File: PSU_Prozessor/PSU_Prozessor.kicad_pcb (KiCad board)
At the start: 2 copper layers, 192.4 x 77 mm, 85 parts, among them IC1 6N138S, J1 ACJS-MHOP, J2 Conn_01x06, J3 FC68148S, J4 USB2066-05-RBHM-15-STB-00-01-A, J7 USB2066-05-RBHM-15-STB-00-01-A, Q1 BC847, Q2 2N7002, Q3 BC847, Q4 2N7002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

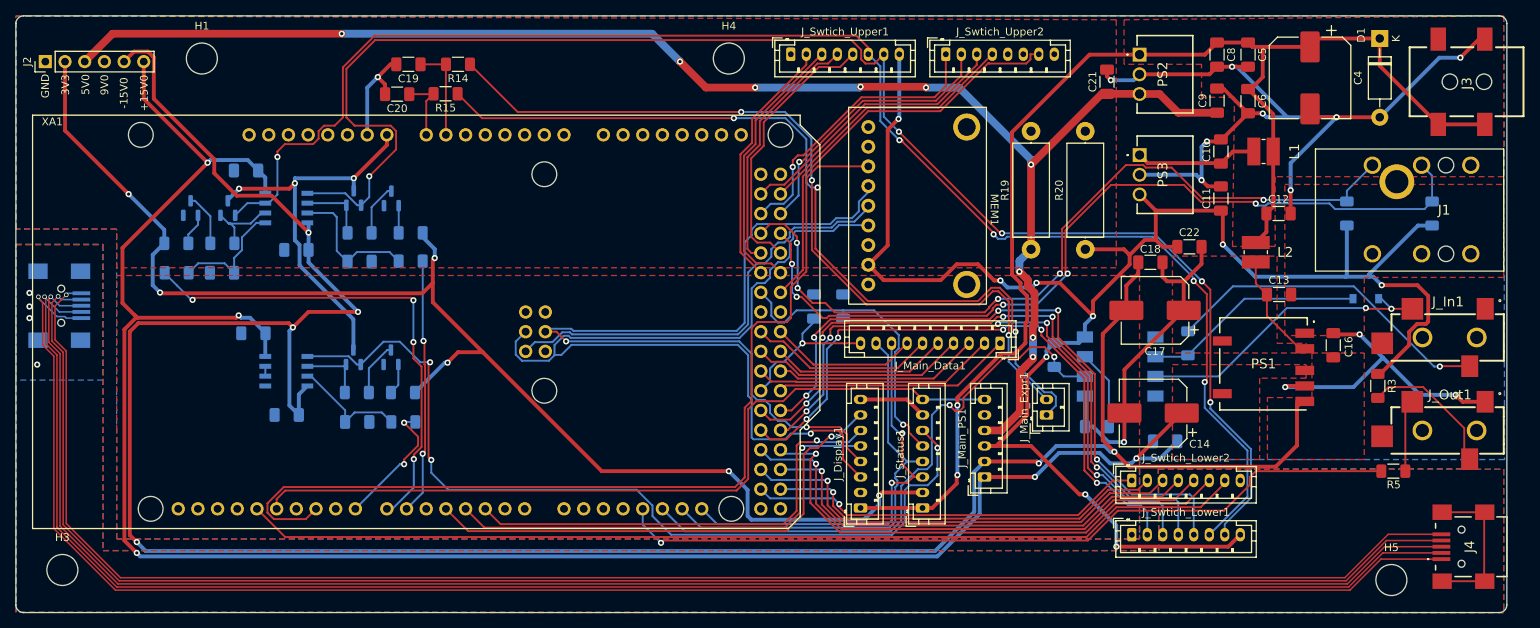
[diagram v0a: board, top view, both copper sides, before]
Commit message: Added 9V supply on PSU for LEDs on switch. Changed FRAM supply
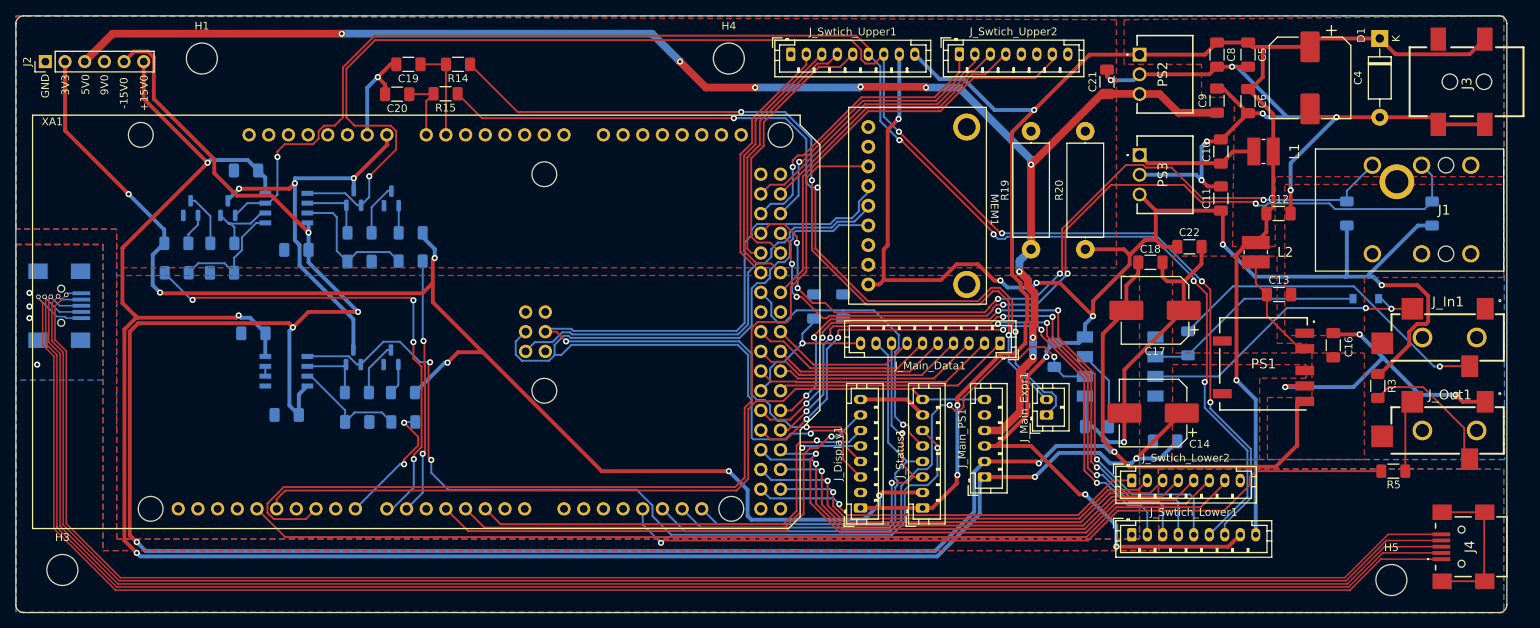
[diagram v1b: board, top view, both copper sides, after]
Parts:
- J_Swtich_Lower1, J_Swtich_Upper1: value Conn_01x08 -> Conn_01x09; footprint Connector_JST:JST_PH_B8B-PH-K_1x08_P2.00mm_Vertical -> Connector_JST:JST_PH_B9B-PH-K_1x09_P2.00mm_Vertical
- moved J_Swtich_Upper2 1.75 mm to (167.8, 67.4)
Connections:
- J3 pad 1: /VDD9V0 -> GND
- J3 pad 2: /VDD9V0 -> GND
- J3 pad 4: GND -> /VDD9V0
- MEM1 pad 8: /VDD3V3 -> unconnected-(MEM1-Pad8)
- MEM1 pad 9: unconnected-(MEM1-Pad9) -> /VDD3V3
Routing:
- net /VDD9V0: track 217.4 -> 271.1 mm, vias 5 -> 7
- net GND: track 217.1 -> 214.1 mm, vias 13 -> 12
- net /OE_Upper: track 53.6 -> 55.4 mm
- net /SW10: track 34.8 -> 36.5 mm
- net /SW9: track 36.1 -> 37.1 mm
- net /SW7: track 37.4 -> 38.1 mm
- net /SW8: track 35.9 -> 36.7 mm
- net /VDD3V3: track 402.3 -> 402.9 mm

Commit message: Changed FRAM pinout, 9V center negative
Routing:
- net /CS_Fram: track 124.1 -> 137.4 mm
- net /VDD3V3: track 402.9 -> 393.1 mm
- net /MOSI: track 109.2 -> 118.7 mm
- net /SCK: track 118.4 -> 124.1 mm

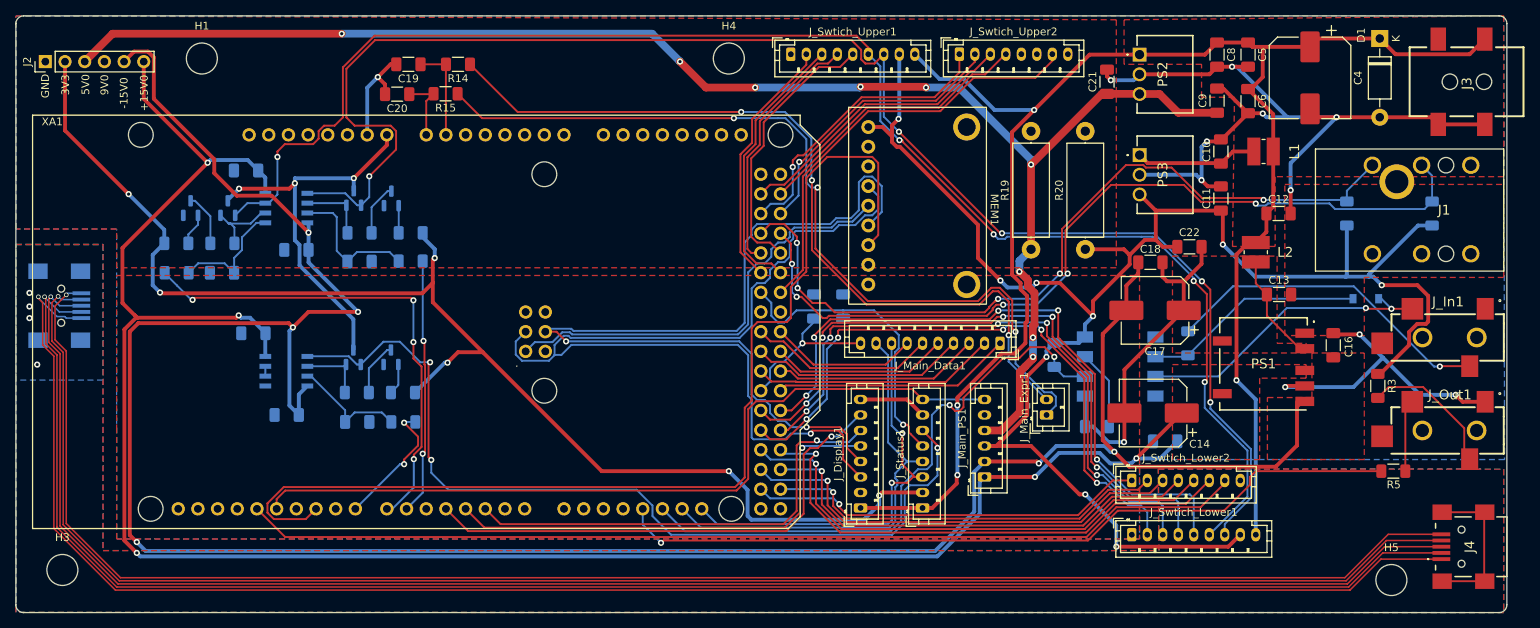
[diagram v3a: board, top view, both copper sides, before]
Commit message: Changed PSU_Processor PCB to adapt changes on Main PCB
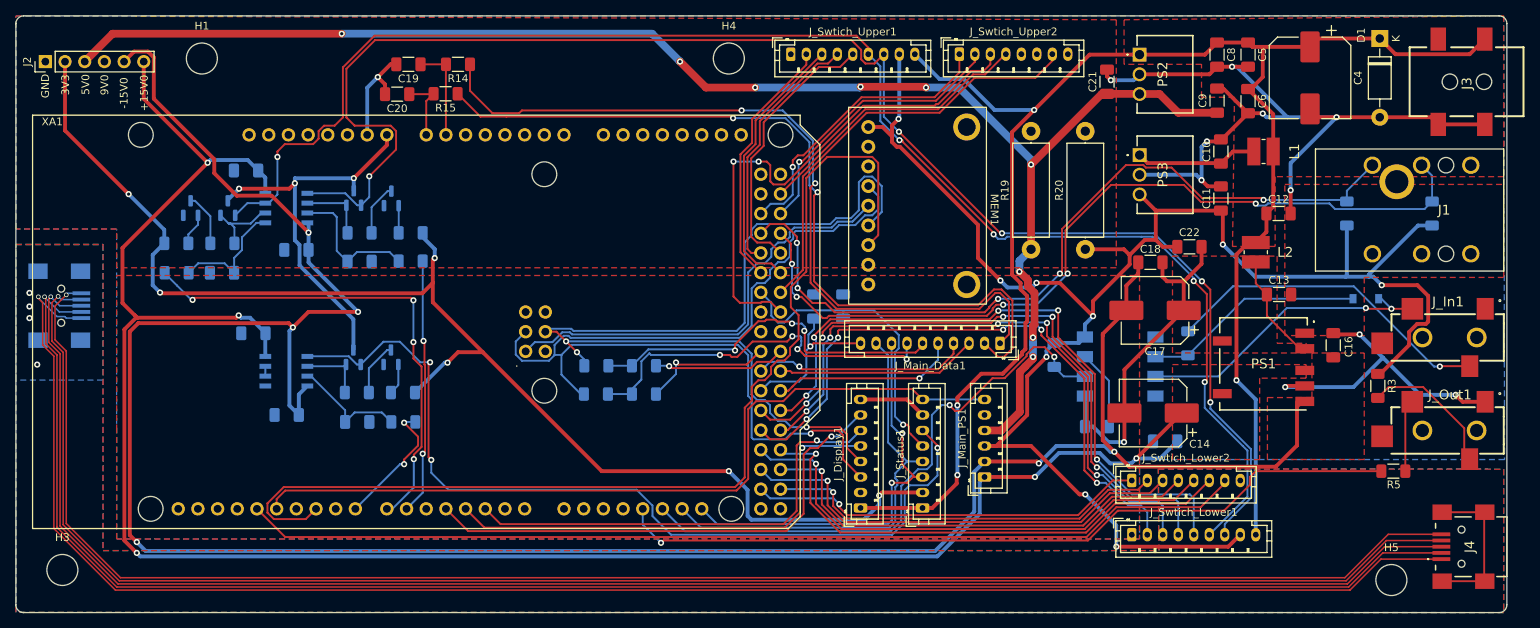
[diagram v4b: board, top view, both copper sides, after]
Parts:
- removed J_Main_Expr1: Conn_01x02, Connector_JST:JST_PH_B2B-PH-K_1x02_P2.00mm_Vertical
- added R21: 0, Resistor_SMD:R_1206_3216Metric_Pad1.30x1.75mm_HandSolder, B.Cu at (127.0, 107.7)
- added R22: 0, Resistor_SMD:R_1206_3216Metric_Pad1.30x1.75mm_HandSolder, B.Cu at (127.0, 111.3)
- added R23: 0, Resistor_SMD:R_1206_3216Metric_Pad1.30x1.75mm_HandSolder, B.Cu at (120.9, 107.7)
- added R24: 0, Resistor_SMD:R_1206_3216Metric_Pad1.30x1.75mm_HandSolder, B.Cu at (120.8, 111.3)
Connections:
- net /SER_Matrix renamed /EN_SPL_Matrix
- J_Main_Data1 pad 1: /En_Matrix -> /Expr_2_In
- J_Main_Data1 pad 2: /OE_Matrix -> /Expr_1_In
- J_Main_Data1 pad 4: /SRCLK_Matrix -> /RCLK_MATRIX
- J_Main_Data1 pad 5: /SRCLR_Matrix -> /SEL_Matrix
- J_Main_Data1 pad 6: /RCLK_Matrix -> Net-(J_Main_Data1-Pad6)
- J_Main_Data1 pad 7: /SER_Out_Matrix -> Net-(J_Main_Data1-Pad7)
- XA1 pad D33: /En_Matrix -> /SEL_Matrix
- XA1 pad D34: /OE_Matrix -> /RCLK_MATRIX
- XA1 pad D36: /SRCLK_Matrix -> /CLK_Matrix
- XA1 pad D37: /SRCLR_Matrix -> /Data_Matrix
- XA1 pad D38: /RCLK_Matrix -> unconnected-(XA1-PadD38)
- XA1 pad D39: /SER_Out_Matrix -> unconnected-(XA1-PadD39)
- XA1 pad D41: unconnected-(XA1-PadD41) -> /SW9
- XA1 pad D52: /SW9 -> unconnected-(XA1-PadD52)
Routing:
- net Net-(J_Main_Data1-Pad7): track 0.00 -> 47.9 mm, vias 0 -> 4
- net Net-(J_Main_Data1-Pad6): track 0.00 -> 47.6 mm, vias 0 -> 3
- net /OE_Matrix: track 31.5 -> 0.00 mm
- net /En_Matrix: track 30.9 -> 0.00 mm
- net /SW9: track 37.1 -> 67.8 mm, vias 0 -> 2
- net /RCLK_MATRIX: track 0.00 -> 27.9 mm, vias 0 -> 1
- net /SRCLK_Matrix: track 27.8 -> 0.00 mm
- net /RCLK_Matrix: track 24.1 -> 0.00 mm
- net /SEL_Matrix: track 0.00 -> 24.1 mm, vias 0 -> 1
- net /SRCLR_Matrix: track 22.9 -> 0.00 mm
- net /SER_Out_Matrix: track 19.2 -> 0.00 mm
- net /Data_Matrix: track 0.00 -> 17.1 mm, vias 0 -> 1
- net /CLK_Matrix: track 0.00 -> 16.8 mm, vias 0 -> 1
- net /SCK: track 124.1 -> 130.1 mm
- net /Expr_1_In: track 110.5 -> 106.0 mm, vias 3 -> 2
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
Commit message: Fixed library imports. Changed psu pcb
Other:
- board text added: "Controller PSU&CPU Rev. 2.0"
- board text removed: "Controller PSU&CPU Rev. 1.0"
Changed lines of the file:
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@@
     (effects (font (size 4 4) (thickness 1)) (justify left mirror))
   )
-  (gr_text "Controller PSU&CPU Rev. 1.0" (at 114.5 98.05) (layer "B.SilkS")
+  (gr_text "Controller PSU&CPU Rev. 2.0" (at 114.5 98.05) (layer "B.SilkS")
     (effects (font (size 2 2) (thickness 0.5)) (justify mirror))
   )
